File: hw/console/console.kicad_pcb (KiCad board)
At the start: 2 copper layers, 156 x 74 mm, 161 parts, among them J1 Batt, J301 USB-C 16P, J401 DM3AT-SF-PEJM5, J501 SPK 8R, J601 FFC-40 0.5mm, J901 UART, Q601 AO3400A, SW1 Движок, SW101 UP, SW102 DOWN, SW103 LEFT, SW104 RIGHT, SW105 SELECT, SW106 START, SW107 A, SW108 B, SW109 C, SW110 D, U1 F133-A, U2 SY8089AAAC, U3 SY8089AAAC, U4 SY8089AAAC, U401 W25Q32JVSSIQ, U5 TP4056, U501 PAM8301, Y1 24 МГц, Y2 32.768 кГц

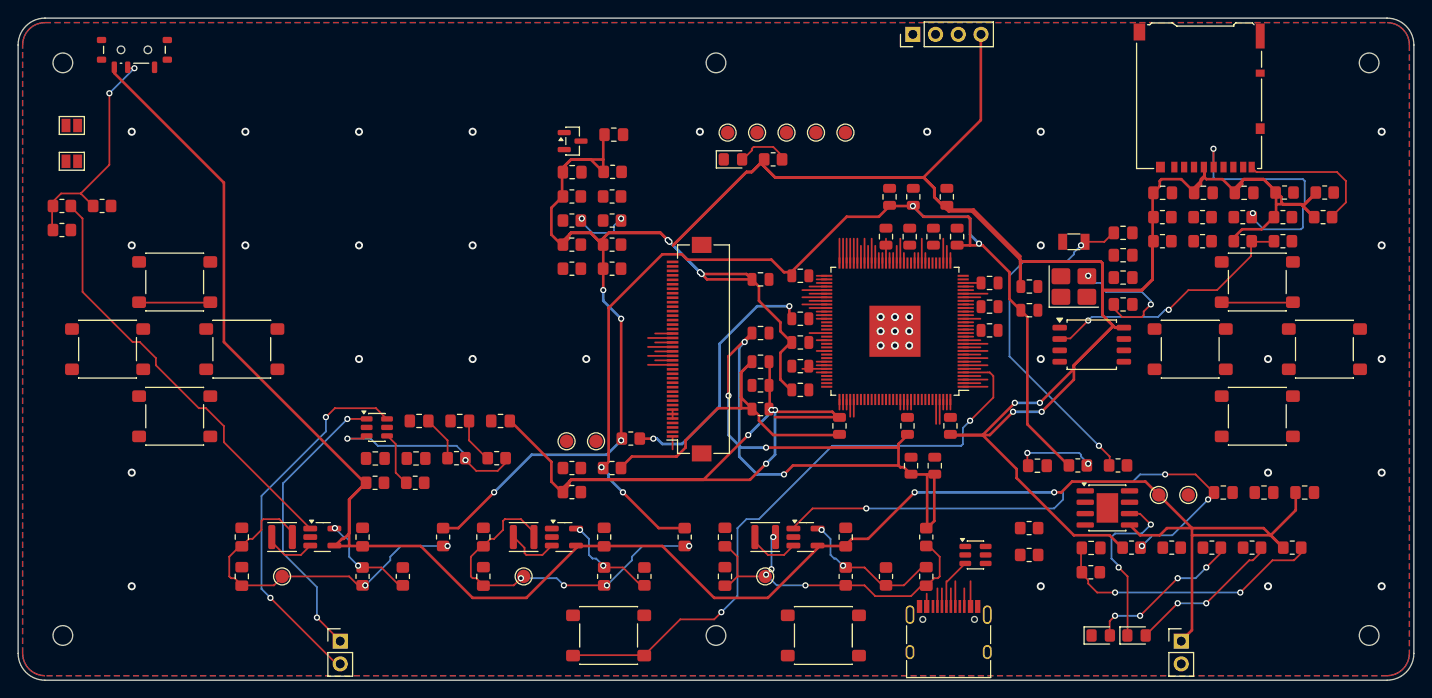
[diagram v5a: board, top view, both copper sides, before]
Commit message: hw: зазор кольца развязки задан по лучу, детали переехали к своим выводам
Веер в 108 лучей был **случайной удачей**, а не результатом. Кольцо развязки
стоит в 0.4 мм от площадок корпуса, и в этот зазор луч не помещается: ему надо
0.4 мм самой короткой длины плюс по 0.2 зазора. А работало оно потому, что я
поменял конденсаторам футпринты, не переразложив кольцо — они остались стоять
по-старому, от больших `HandSolder`, то есть дальше. Первый же честный прогон
`pcb04_fine.py` вернул их на место, и веер упал до 66.

Теперь зазор кольца задан по делу: 1.1 мм. Веер 108 лучей воспроизводится из
скриптов, а не держится на том, чего я не заметил.

Заодно бездомные детали переехали к своим выводам. `JP1` (RESET) и `JP301`
(FEL) стояли в левом углу платы «где не мешают», а их цепи тянулись на 119 и
125 мм. `R802` держит опору калибровки DDR и по даташиту обязана стоять
вплотную к выводу 47 — лежала в 44 мм. Делители разрешения баков разъехались
каждый к своему баку.

Разбор длинных связей: 57 штук длиннее 25 мм несут 2705 мм — почти всю длину
платы. Крестовина среди них неисправима размещением: её линии выходят у чипа
справа, а кнопки на левом краю по эргономике. Это правка схемы.

Co-Authored-By: Claude Opus 5 <noreply@anthropic.com>
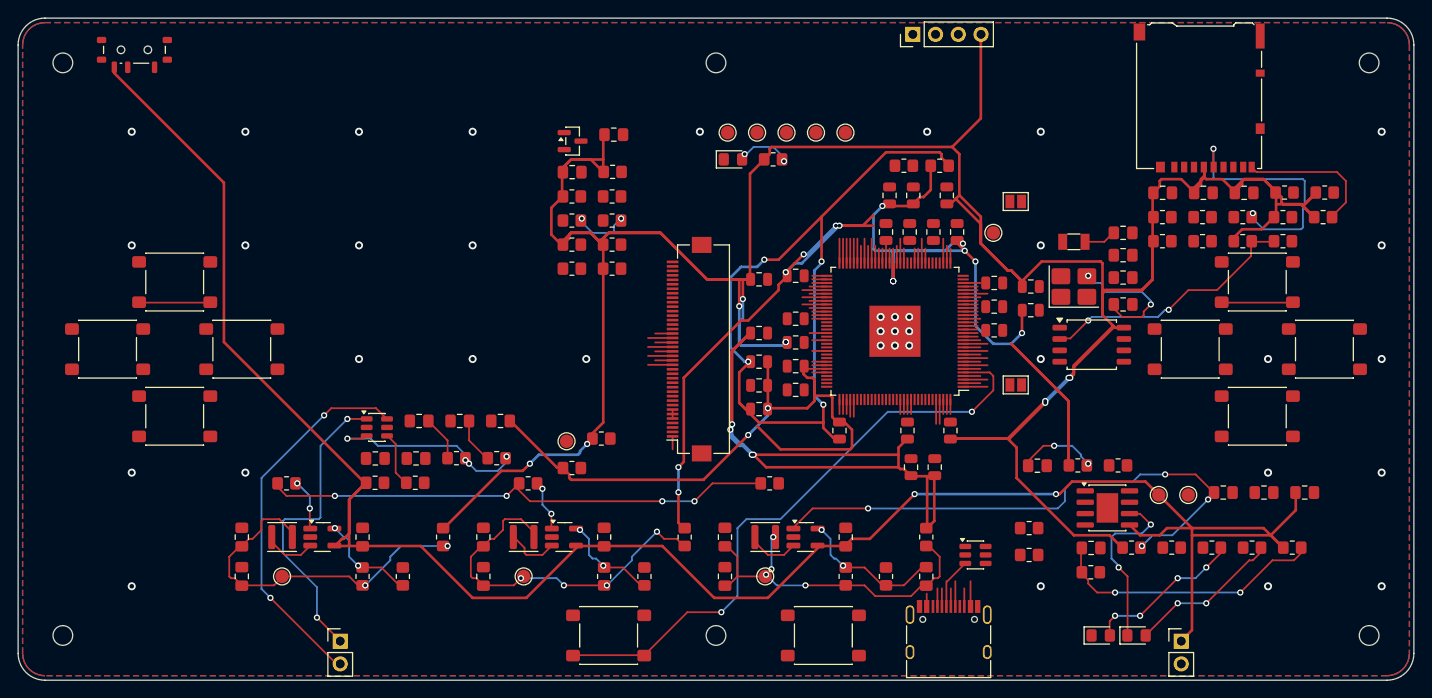
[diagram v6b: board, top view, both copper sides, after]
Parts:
- moved JP301 108.4 mm to (161.5, 81.0)
- moved JP1 105.8 mm to (161.5, 60.5)
- moved R9 84.0 mm to (134.0, 92.0)
- moved R8 56.8 mm to (107.0, 92.0)
- moved TP801 53.1 mm to (159.0, 64.0)
- moved R802 50.2 mm to (149.0, 56.5)
- moved R803 49.8 mm to (153.0, 56.5)
- moved R7 39.9 mm to (80.0, 92.0)
- moved TP802 3.29 mm to (111.3, 87.3)
- moved R801 3.29 mm to (115.2, 87.0)
- moved R804 2.69 mm to (111.9, 90.3)
- moved C801 0.52 mm to (136.9, 81.5)
- moved C804 0.52 mm to (136.9, 76.2)
- moved C807 0.52 mm to (159.1, 74.9)
- moved C812 0.52 mm to (136.9, 68.8)
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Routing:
- net AVCC: track 43.3 -> 88.9 mm, vias 0 -> 4
- net +3V3: track 449.9 -> 404.4 mm, vias 12 -> 10
- net EN_3V3: track 48.0 -> 5.78 mm, vias 0 -> 2
- net +1V8: track 132.5 -> 170.0 mm, vias 4 -> 14
- net X32KOUT: track 40.7 -> 5.24 mm, vias 2 -> 0
- net /PWR_EN: track 26.0 -> 57.3 mm, vias 2 -> 4
- net VCC-TVOUT: track 30.1 -> 1.62 mm, vias 2 -> 0
- net AGND: track 92.6 -> 74.7 mm, vias 4 -> 2
- net EN_1V8: track 0.00 -> 5.66 mm, vias 0 -> 2
- net Net-(J501-Pin_1): track 32.6 -> 34.9 mm
- net KEY-SELECT: track 70.3 -> 68.8 mm
- net Net-(D901-A): track 5.91 -> 6.59 mm, vias 0 -> 2
- net Net-(U501-IN): track 22.9 -> 23.5 mm, vias 2 -> 4
- net DXIN: track 15.9 -> 16.4 mm
- net X32KIN: track 1.12 -> 1.62 mm
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
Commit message: hw: разъём шлейфа — высота важнее близости, и это стоило 14 пересечений
Взялся за дисплей как за самое дорогое: 23 линии, четверть платы. Перебрал
место и угол разъёма (`lcd_place.py`, новый) при трёх закреплённых
ограничениях — вылет шлейфа по изнанке панели (43.72 мм) не пускает разъём
правее x ≈ 79.7; кольцо развязки занимает коридор до корпуса; окно смотрит
влево, откуда приходит шлейф.

Оказалось, что решает не близость к чипу, а **высота**. Разъём стоял на
y = 37, по середине корпуса, и шина была 464 мм с 27 пересечениями. На
y = 31.5, напротив ленты выводов 52…76, — **415 мм и 13 пересечений**. Даром:
пересечений courtyard ноль, развязка на местах.

Порядок бит данных при этом наш: панель кормим своим кодом, перестановка
вносится в палитру и в команды i8080 один раз. Назначение считается венгерским
алгоритмом там же, в `lcd_place.py`.

Проверено и отвергнуто, с числами:

* **разъём наискось, под 105°** — ряд лицом к углу корпуса, 228 мм и **одно**
  пересечение. Занимает весь левый бок, кольцу развязки приходится уходить за
  углы: двенадцать конденсаторов отъезжают от своих выводов на 9…18 мм,
  кварцы на 17. Развязка на 18 мм от вывода питания у 480-мегагерцевого чипа —
  это уже не развязка;
* **разворот панели на 180°** (шлейф справа, окно вправо) — шина 186 мм, но
  17 пересечений против 13. Короче, да дороже: пересечение это переходная, а
  каждая переходная у нас паяется вручную с двух сторон;
* **сдвиг чипа влево** — сам по себе не даёт ничего: кольцо развязки едет
  вместе с ним, и разъём упирается в него на том же расстоянии.

Заодно кварцы и флешка встали в координатах от середины корпуса, а не от угла
платы: они обязаны ехать за чипом, а при первом же его сдвиге молча остались
на месте в двадцати миллиметрах от своих выводов.

Co-Authored-By: Claude Opus 5 <noreply@anthropic.com>
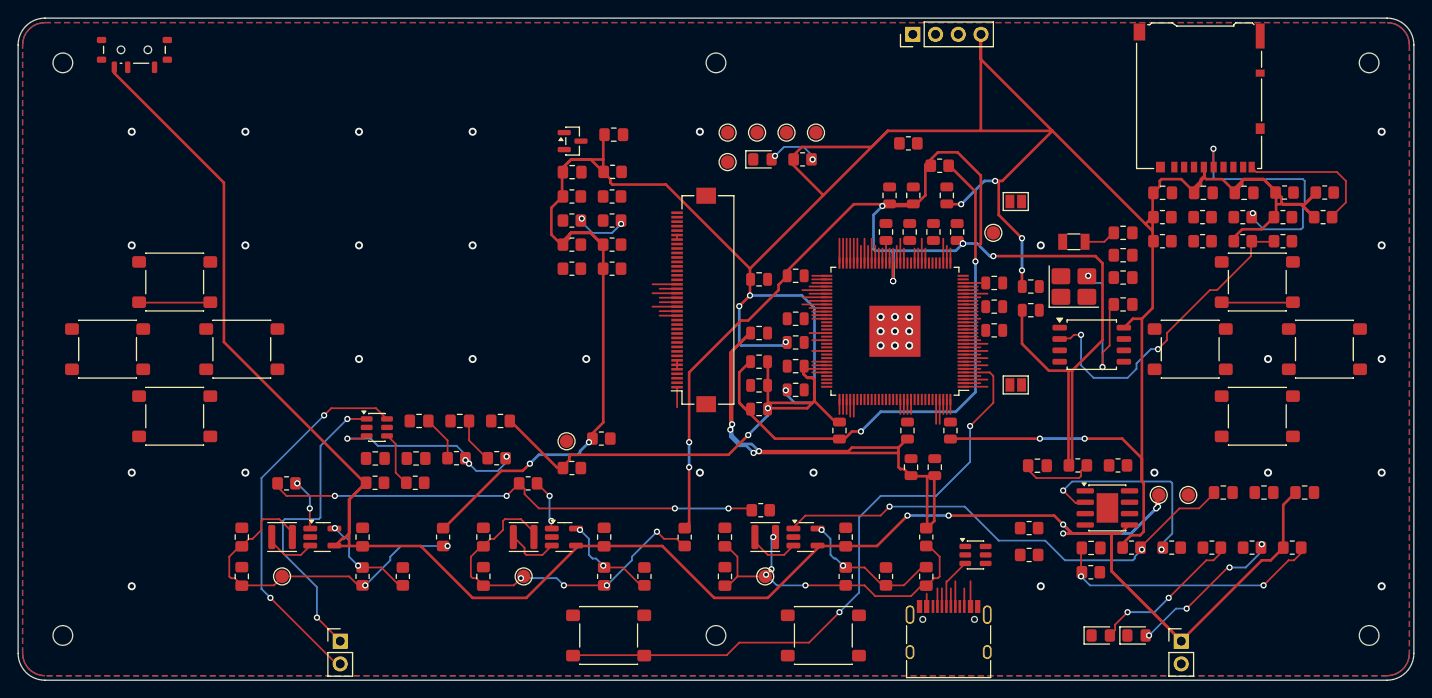
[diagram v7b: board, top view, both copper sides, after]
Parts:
- moved TP905 13.6 mm to (129.3, 56.1)
- moved J601 5.52 mm to (125.5, 71.5)
- moved R901 3.29 mm to (137.7, 55.8)
- moved D901 3.29 mm to (133.2, 55.8)
- moved R9 3.16 mm to (133.0, 95.0)
- moved R802 2.55 mm to (149.5, 54.0)
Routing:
- net Net-(U5-PROG): track 0.00 -> 23.9 mm, vias 0 -> 2
- net VSYS: track 234.0 -> 256.6 mm, vias 2 -> 6
- net AVCC: track 88.9 -> 67.1 mm, vias 4 -> 2
- net Net-(D2-K): track 19.6 -> 0.00 mm, vias 2 -> 0
- net +3V3: track 404.4 -> 396.3 mm, vias 10 -> 12
- net AGND: track 74.7 -> 66.6 mm
- net EN_0V9: track 62.0 -> 54.3 mm, vias 4 -> 2
- net SPI0-MISO: track 31.0 -> 37.8 mm
- net +1V8: track 170.0 -> 174.2 mm, vias 14 -> 8
- net DXIN: track 16.4 -> 20.5 mm
- net KEY-SELECT: track 68.8 -> 72.4 mm
- net /PWR_EN: track 57.3 -> 56.0 mm
- net RESET: track 11.9 -> 11.1 mm, vias 2 -> 0
- net LCD-DB3: track 5.47 -> 4.67 mm
- net Net-(D2-A): track 17.3 -> 18.1 mm, vias 2 -> 4
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
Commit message: hw: порядок бит на шлейфе выбран по разводке, и лучи разъёма смотрят на чип
Шина дисплея не разводилась совсем: пущенная первой по пустой плате, она
сходилась на шесть связей из тридцати шести. Разобрал до дна — оказалось три
причины, все мои.

**Лучи разъёма смотрели от чипа.** Общее правило «наружу от середины детали»
верно для корпуса с четырьмя сторонами, а у однорядного разъёма ведёт в
сторону, откуда приходит шлейф, — то есть влево, а чип справа. Вся шина
разворачивалась вокруг 26-миллиметрового корпуса. Меди под корпусом `FH12`
ничего не запрещает (зон правил у него нет, в отличие от лотка microSD), и
теперь лучи идут вправо, под корпус, прямо к чипу.

**Трассировщик целился в площадку, а не в конец луча.** Площадки мелкого шага
замурованы соседями — для того лучи и выведены, — но цель оставалась
площадкой, и лучи не помогали вовсе.

**Порядок бит был «в лоб».** Линии выходят у чипа лентой вдоль верхнего левого
угла, и при порядке по возрастанию шина обязана сама себя перекрестить в
десятимиллиметровом коридоре. Поодиночке каждая линия разводится за секунду,
вместе — не проходят. Порядок бит у нас свой: панель кормит наш же код,
перестановка вносится один раз в палитру и один раз в таблицу команд i8080.
Соответствие посчитано венгерским алгоритмом по координатам площадок:
`DB0…DB7` развёрнуты целиком, `DB10` и `DB11` поменялись местами. Шина 390 мм
и 6 пересечений вместо 415 и 13.

Ещё: кольцо развязки уступает шине горизонтальный коридор шириной по числу
линий (23 × 0.4 + запас), а конденсаторы, которым выпало это место, сдвигаются
ВДОЛЬ бока, а не уезжают за угол. Цена — четыре штуки в 7.7…12 мм от своих
выводов.

И новый шаг конвейера `pcb00_nets.py`: переносит цепи со схемы на плату из
нетлиста `kicad-cli`. Менять, какой вывод в какой цепи, — обычное проектное
решение, а «Update PCB from Schematic» живёт только в окне KiCad; без этого
каждая такая правка требовала бы ручного шага и молча ломалась бы, если про
него забыть.

Итог: неподключённых 140 против 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
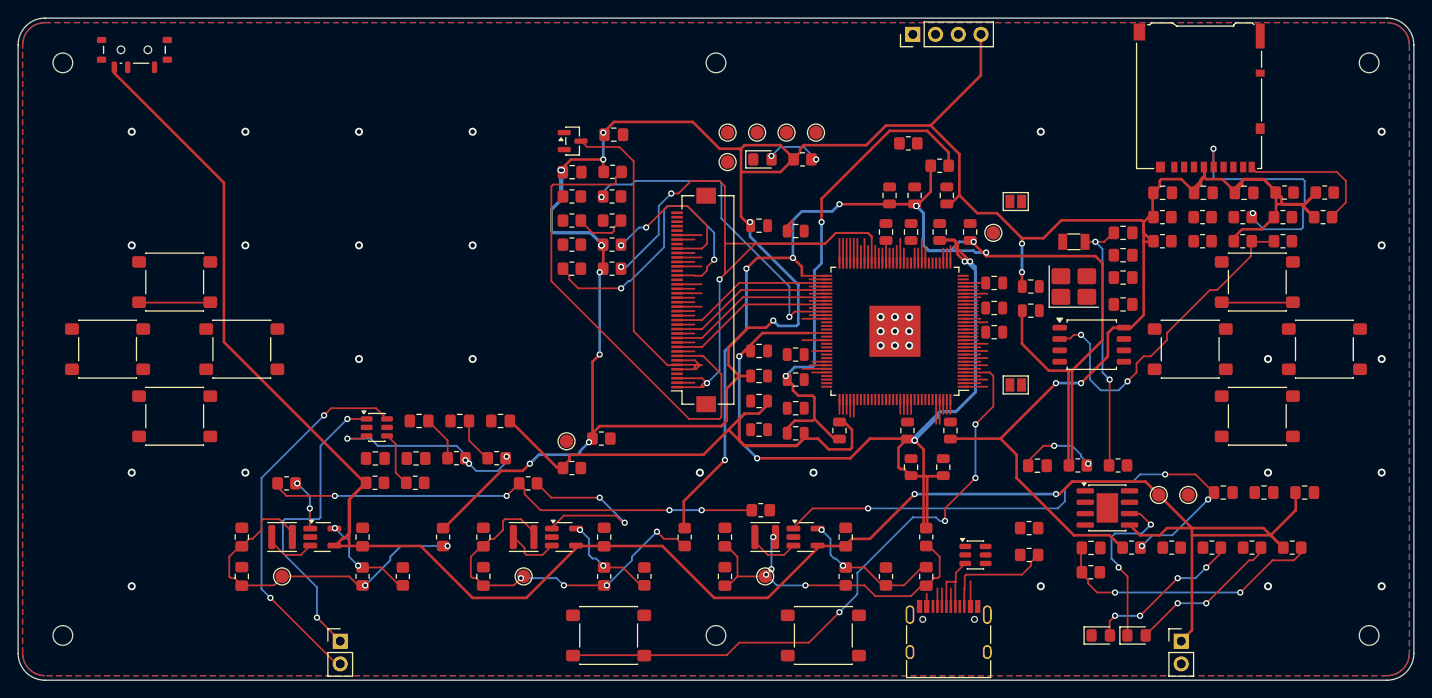
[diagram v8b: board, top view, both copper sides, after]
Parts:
- moved C801 6.04 mm to (132.8, 86.0)
- moved C803 6.00 mm to (132.8, 63.2)
- moved C827 5.65 mm to (132.8, 82.8)
- moved C804 5.55 mm to (132.8, 80.0)
- moved C812 5.00 mm to (136.9, 63.8)
- moved C823 4.90 mm to (136.9, 86.4)
- moved C826 4.82 mm to (136.9, 83.6)
- moved C824 4.55 mm to (136.9, 80.4)
- moved C820 4.00 mm to (136.9, 77.6)
- moved C816 2.00 mm to (132.8, 77.2)
- moved C806 1.45 mm to (156.4, 63.9)
- moved C813 0.95 mm to (153.4, 90.2)
- moved C814 0.70 mm to (153.0, 63.9)
- moved C807 0.20 mm to (159.1, 75.1)
- moved C810 0.15 mm to (149.8, 63.9)
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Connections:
- J601 pad 17: LCD-DB0 -> LCD-DB7
- J601 pad 18: LCD-DB1 -> LCD-DB6
- J601 pad 19: LCD-DB2 -> LCD-DB5
- J601 pad 20: LCD-DB3 -> LCD-DB4
- J601 pad 21: LCD-DB4 -> LCD-DB3
- J601 pad 22: LCD-DB5 -> LCD-DB2
- J601 pad 23: LCD-DB6 -> LCD-DB1
- J601 pad 24: LCD-DB7 -> LCD-DB0
- J601 pad 27: LCD-DB10 -> LCD-DB11
- J601 pad 28: LCD-DB11 -> LCD-DB10
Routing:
- net LCD-IM: track 4.97 -> 87.3 mm, vias 0 -> 4
- net LCD-LEDA: track 0.00 -> 55.5 mm
- net +0V9: track 93.3 -> 134.5 mm, vias 4 -> 6
- net LCD-LEDK: track 1.05 -> 41.3 mm
- net LCD0-CLK: track 1.62 -> 37.2 mm, vias 0 -> 2
- net LCD-RST: track 2.72 -> 36.5 mm, vias 0 -> 2
- net X32KOUT: track 5.24 -> 30.9 mm, vias 0 -> 2
- net Net-(U5-PROG): track 23.9 -> 0.00 mm, vias 2 -> 0
- net VSYS: track 256.6 -> 234.0 mm, vias 6 -> 2
- net +3V3: track 396.3 -> 375.7 mm, vias 12 -> 16
- net Net-(D2-K): track 0.00 -> 19.6 mm, vias 0 -> 2
- net DXIN: track 20.5 -> 1.62 mm, vias 2 -> 0
- net LCD-CS: track 1.62 -> 19.6 mm, vias 0 -> 2
- net LCD-DB8: track 1.62 -> 18.4 mm
- net LCD-DB14: track 2.72 -> 18.7 mm
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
